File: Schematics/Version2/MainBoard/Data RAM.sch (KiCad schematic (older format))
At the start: 1 part, among them J27 Data RAM Connector

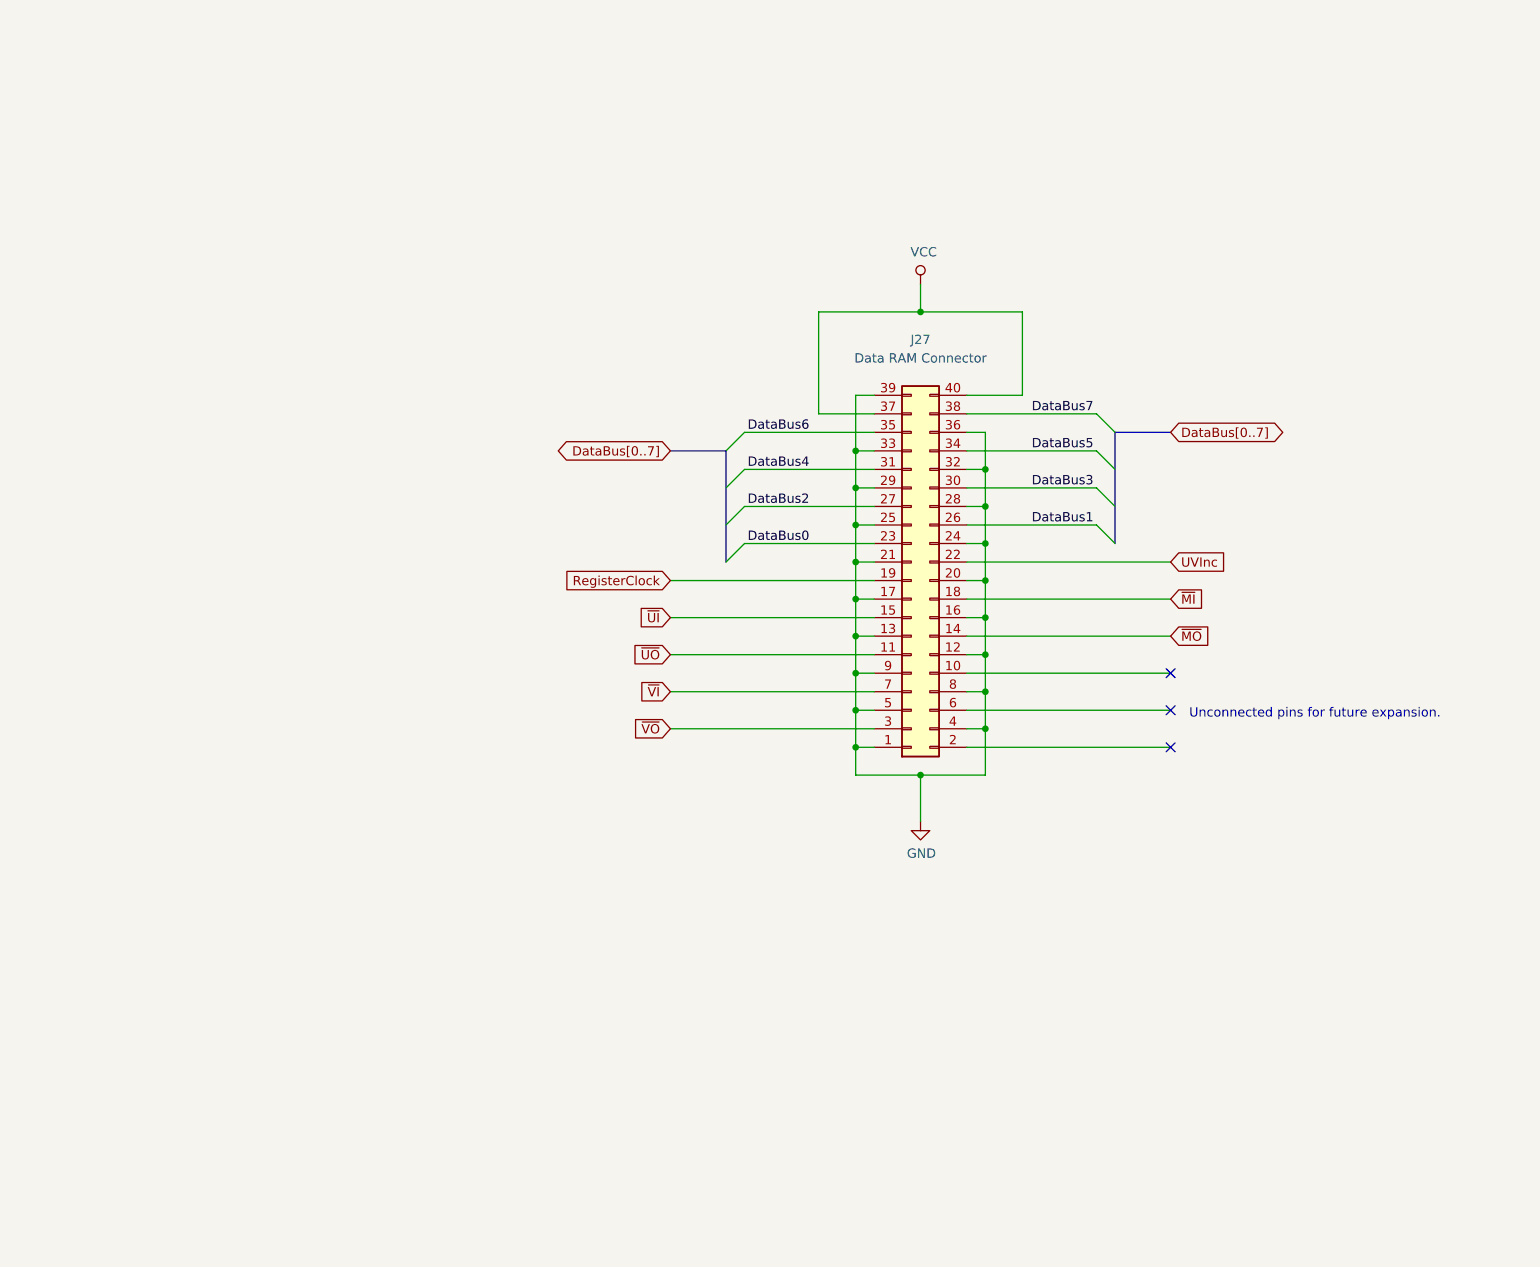
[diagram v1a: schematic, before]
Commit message: Merge branch "version2b".
This is a new version of the computer which incorporates a number of
improvements:
  * Uses a four layer PCB instead of six.
  * Replaced the clock with a new circuit. This is simpler, but allows for
    an external clock to be attached.
  * Changes to the ALU to have it operate over two clock cycles instead of
    one. This fixes a timing issue which makes the ALU unreliable at 10MHz.
  * Replaced instruction RAM with dual port SRAM.
  * Replaced the physical connector for expansion cards to interleave
    signals with ground.
  * Added places where components can be attached to provide AC termination
    of the data bus, should this be necessary.
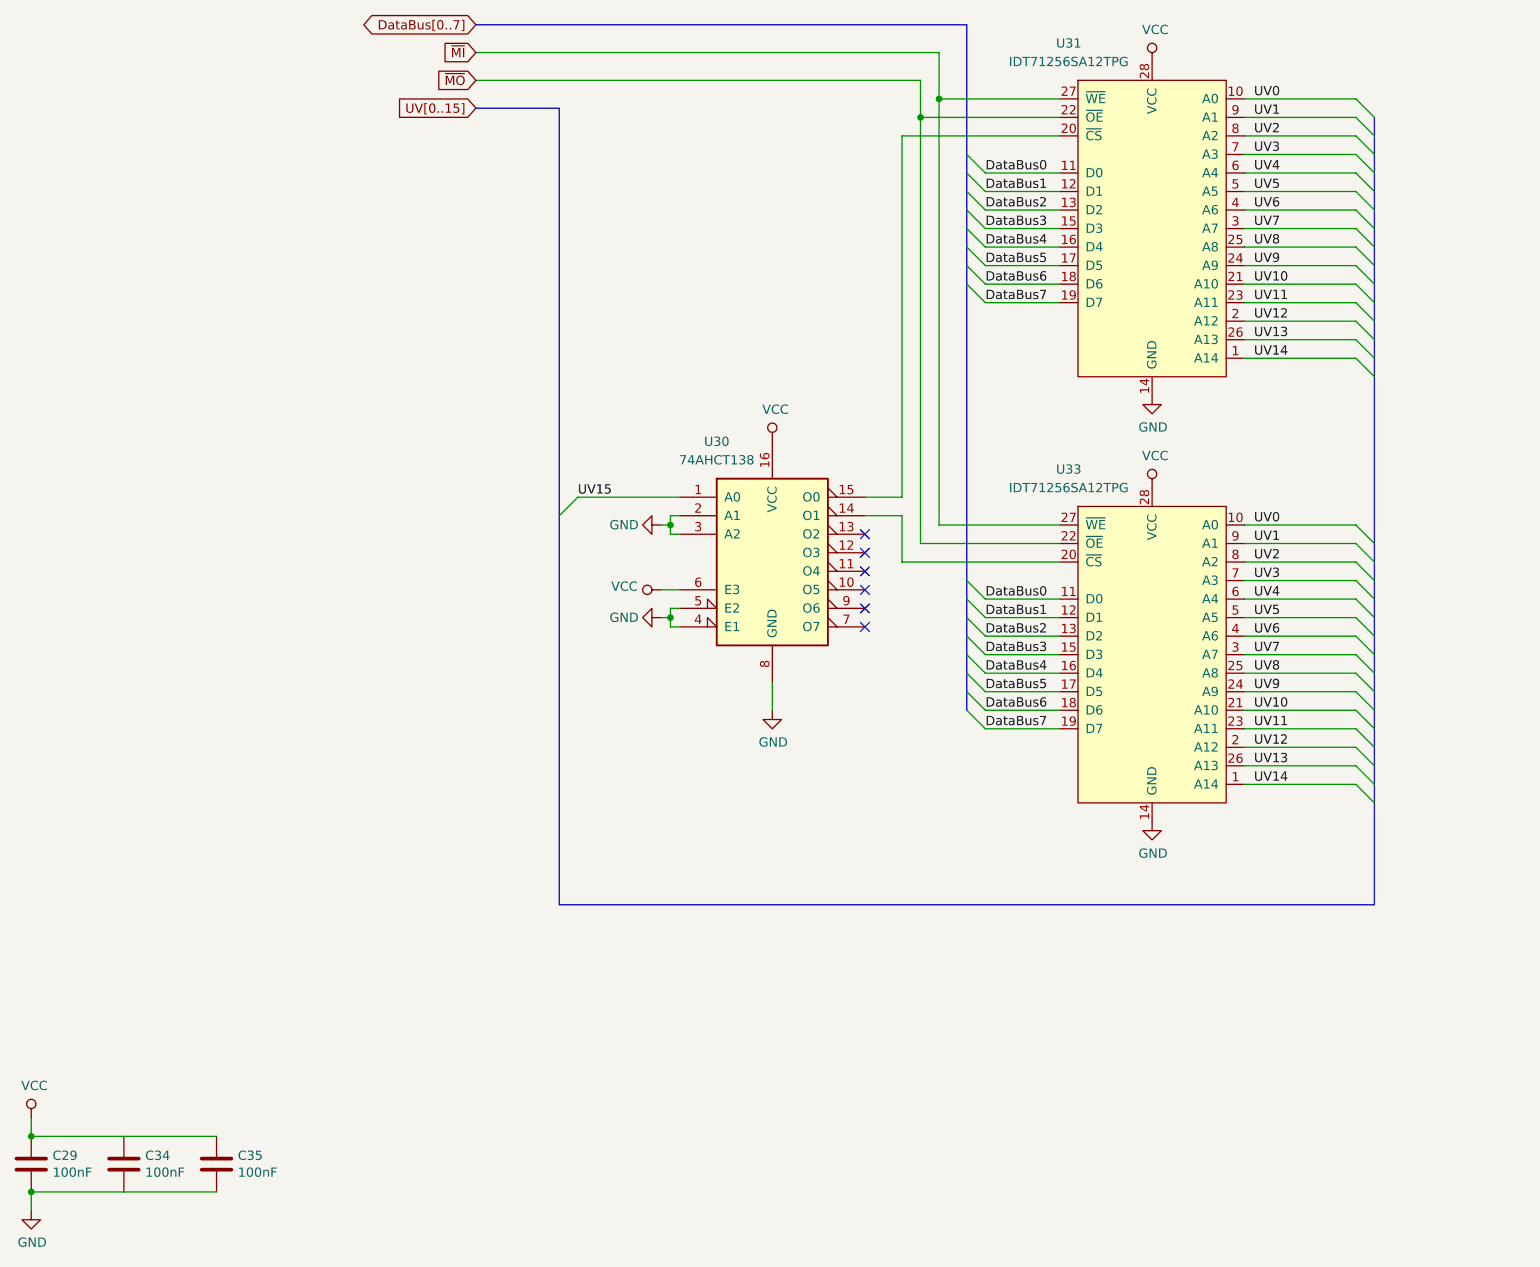
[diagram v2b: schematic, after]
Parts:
- removed J27: Data RAM Connector, Connector_PinSocket_2.54mm:PinSocket_2x20_P2.54mm_Vertical, symbol Connector_Generic:Conn_02x20_Odd_Even
- added C29, C34, C35: 100nF, Capacitor_THT:C_Disc_D4.3mm_W1.9mm_P5.00mm, symbol Device:C
- added U30: 74AHCT138, Package_DIP:DIP-16_W7.62mm, symbol 74xx:74LS138
- added U31, U33: IDT71256SA12TPG, Package_DIP:DIP-28_W7.62mm_Socket, symbol Memory_RAM:IDT71256SA12TPG
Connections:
- net DataBus0: now also U31.11 (D0), U33.11 (D0)
- net DataBus1: now also U31.12 (D1), U33.12 (D1)
- net DataBus2: now also U31.13 (D2), U33.13 (D2)
- net DataBus3: now also U31.15 (D3), U33.15 (D3)
- net DataBus4: now also U31.16 (D4), U33.16 (D4)
- net DataBus5: now also U31.17 (D5), U33.17 (D5)
- net DataBus6: now also U31.18 (D6), U33.18 (D6)
- net DataBus7: now also U31.19 (D7), U33.19 (D7)
- net GND: now also C29.2, C34.2, C35.2, U30.2 (A1), U30.3 (A2), U30.4 (E1), U30.5 (E2), U30.8 (GND), U31.14 (GND), U33.14 (GND)
- net VCC: now also C29.1, C34.1, C35.1, U30.16 (VCC), U30.6 (E3), U31.28 (VCC), U33.28 (VCC)
- net ~MI: now also U31.27 (~WE), U33.27 (~WE)
- net ~MO: now also U31.22 (~OE), U33.22 (~OE)
- new net: U30.14 (O1), U33.20 (~CS)
- new net: U30.15 (O0), U31.20 (~CS)
- new net UV0: U31.10 (A0), U33.10 (A0)
- new net UV1: U31.9 (A1), U33.9 (A1)
- new net UV10: U31.21 (A10), U33.21 (A10)
- new net UV11: U31.23 (A11), U33.23 (A11)
- new net UV12: U31.2 (A12), U33.2 (A12)
- new net UV13: U31.26 (A13), U33.26 (A13)
- new net UV14: U31.1 (A14), U33.1 (A14)
- new net UV15: U30.1 (A0)
- new net UV2: U31.8 (A2), U33.8 (A2)
- new net UV3: U31.7 (A3), U33.7 (A3)
- new net UV4: U31.6 (A4), U33.6 (A4)
- new net UV5: U31.5 (A5), U33.5 (A5)
- new net UV6: U31.4 (A6), U33.4 (A6)
- new net UV7: U31.3 (A7), U33.3 (A7)
- new net UV8: U31.25 (A8), U33.25 (A8)
- new net UV9: U31.24 (A9), U33.24 (A9)
- no-connect marks 3 -> 6
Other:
- note removed: "Unconnected pins for future expansion."
